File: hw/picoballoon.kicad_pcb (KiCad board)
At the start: 2 copper layers, 51.2 x 20 mm, 28 parts, among them J1 Conn_ARM_JTAG_SWD_10, J4 u.fl, U1 TPS610994YFFR, U2 K32L2B21VLH0A, U3 L96-M33, U4 INNOCOMM-SN10-11, U5 MS561101BA03-50

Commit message: tracks cleanup
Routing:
- net +BATT: track 28.0 -> 29.2 mm
- net +3V3: track 85.3 -> 85.8 mm
- net /RF_SPI_SDI: track 15.7 -> 16.2 mm

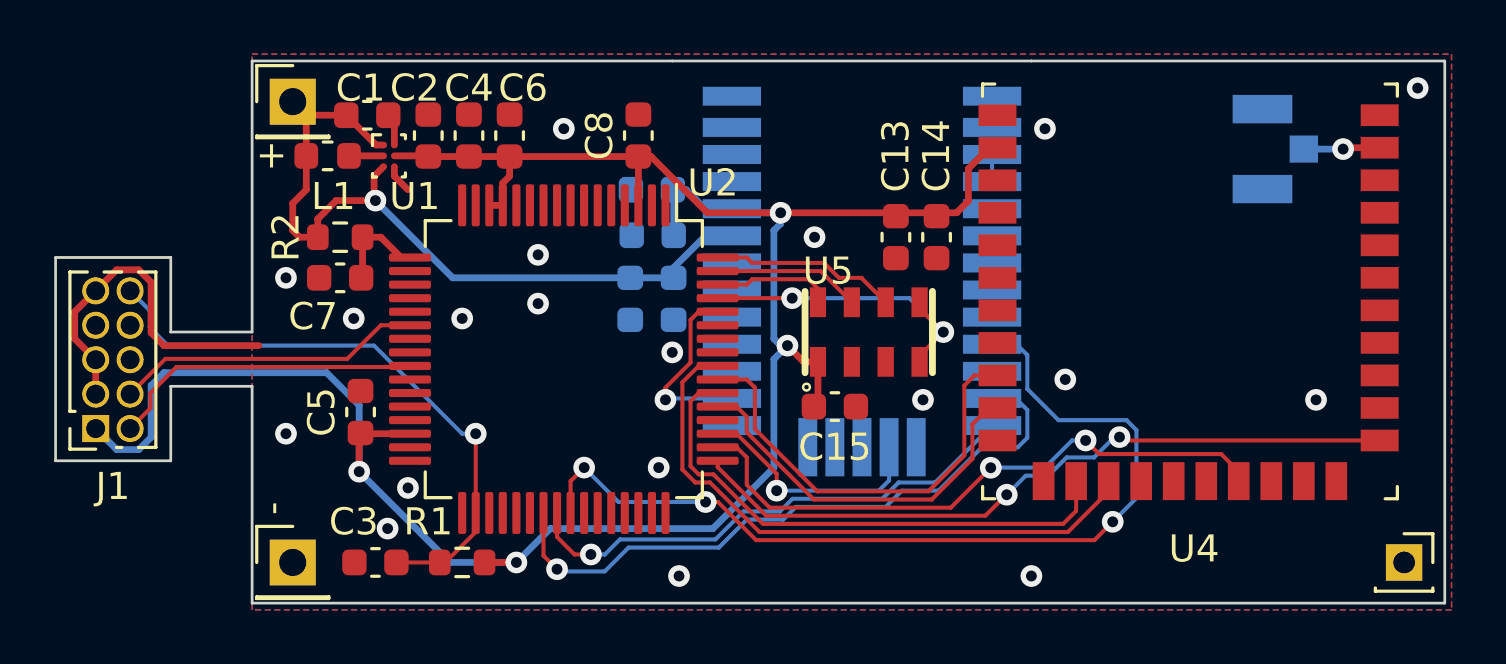
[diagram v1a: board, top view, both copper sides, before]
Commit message: change gps reset pin
cleanup pcb tracks
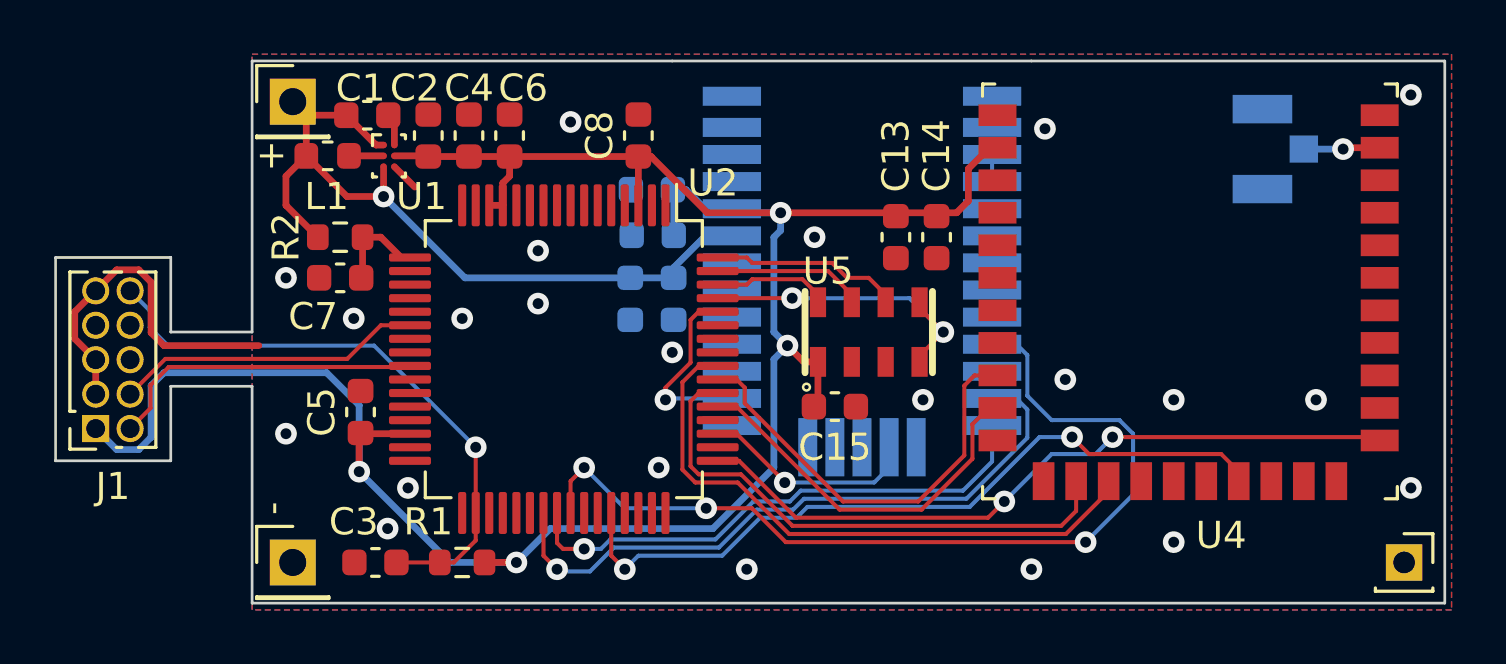
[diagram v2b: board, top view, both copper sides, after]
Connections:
- net /GNSS_RESET renamed /~{GNSS_RESET}
- U2 pad 44: unconnected-(U2-PTC1/LLWU_P6/RTC_CLKIN-Pad44) -> /~{RF_RESET}
- U2 pad 50: /~{RF_RESET} -> unconnected-(U2-VLL1/PTC21-Pad50)
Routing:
- net /~{RF_RESET}: track 22.6 -> 27.8 mm
- net /GNSS_WU: track 8.94 -> 8.07 mm
- net /GNSS_RX: track 19.2 -> 19.9 mm
- net GND: vias 19 -> 22

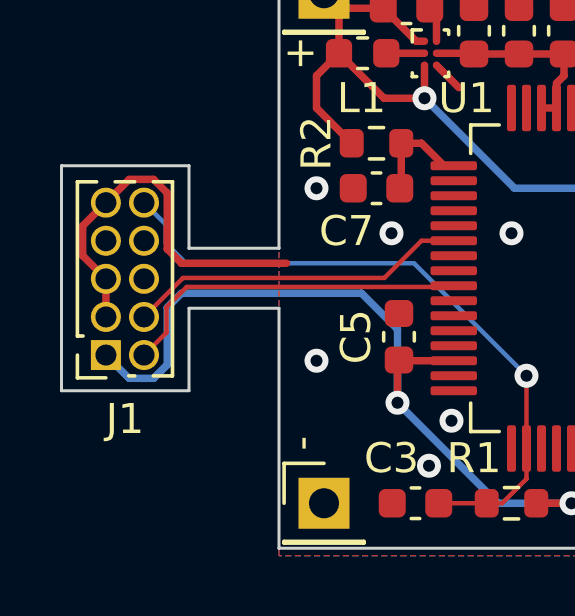
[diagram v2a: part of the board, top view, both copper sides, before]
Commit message: fix swd footprint
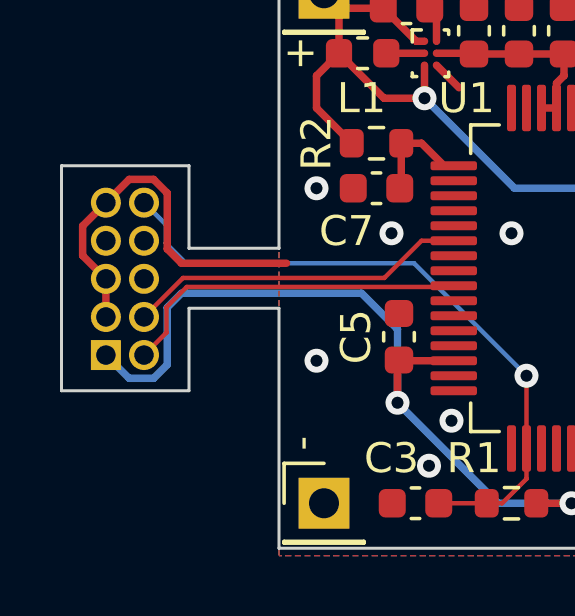
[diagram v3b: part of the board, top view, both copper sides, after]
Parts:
- J1: footprint Connector_PinSocket_1.27mm:PinSocket_2x05_P1.27mm_Vertical -> Connector_PinHeader_1.27mm:PinHeader_2x05_P1.27mm_Vertical; moved to B.Cu
- turned J1 to 0 degrees
